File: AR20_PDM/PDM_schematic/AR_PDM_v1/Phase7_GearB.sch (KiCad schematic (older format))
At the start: 12 parts, among them Q7 BTS50025-1TAD, U11 INA233

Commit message: Alpha version DONE! - Gerber files generated
- Tweeked
- checked and re cheked
- added all missing components
- Created a really nice silkscreen
- Ready To Test
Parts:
- renumbered C12 to C37, C_out6 to C38, C13 to C39, C14 to C40, C15 to C41, Q7 to Q8, R12 to R35, R_in6 to R36, R_sense6 to R37, R13 to R38, R_Shunt10 to R39, U11 to U8

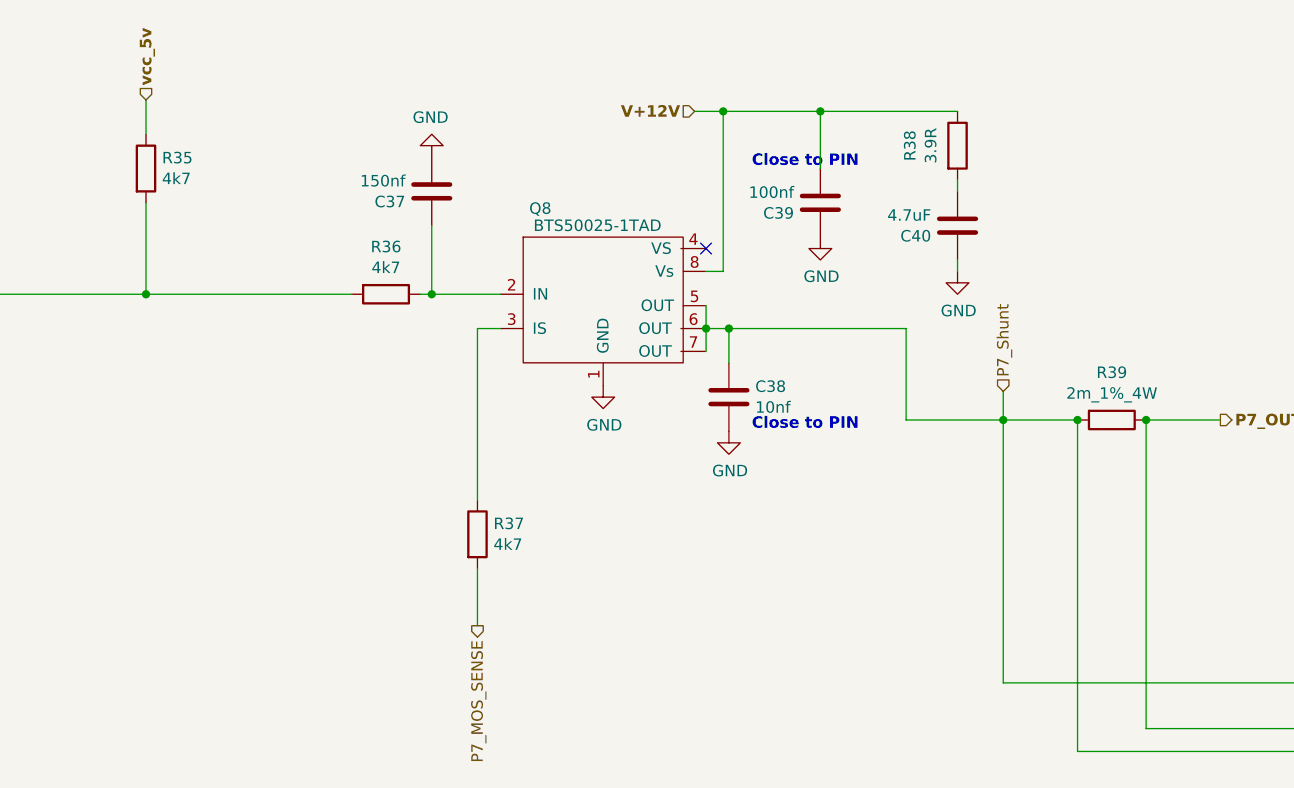
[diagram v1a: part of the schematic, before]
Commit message: Fixed wrong resistors, mos sense. Gerber files updated
- removed all R_is_protection resistors on each mosfet line
- added one R_is_protection resistors to mos_sense_all
ps, mux N-fets, does not need overvoltage protection. 60 volt tolerant.
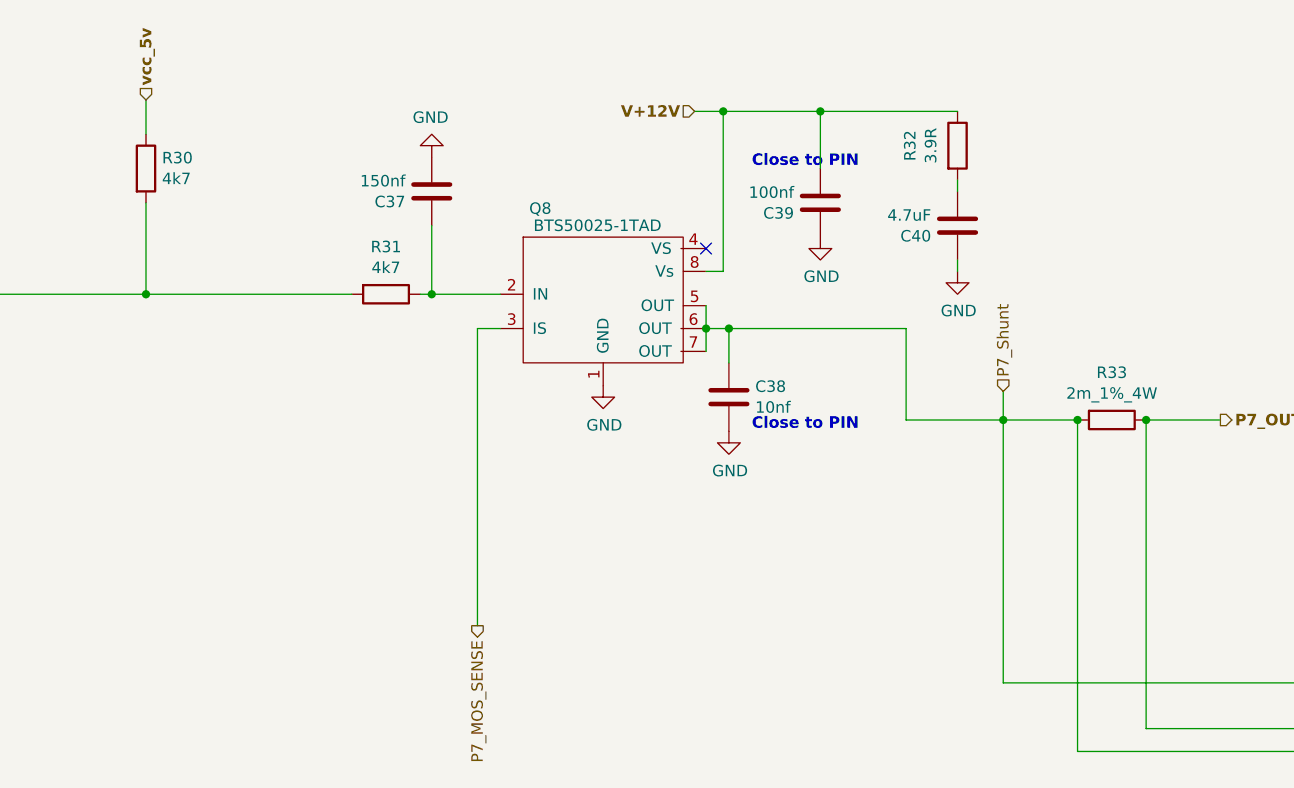
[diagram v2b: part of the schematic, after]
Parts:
- removed R37: 4k7, Resistor_SMD:R_0603_1608Metric, symbol AR20_PDM_v1-rescue:R-Device
- renumbered R35 to R30, R36 to R31, R38 to R32, R39 to R33
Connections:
- net P7_MOS_SENSE: now also Q8.3 (IS)
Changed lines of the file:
@@
 AR Path="/5E0FCFDC/5DAAC1B1" Ref="R?"  Part="1"
 AR Path="/5E0FDCCC/5DAAC1B1" Ref="R?"  Part="1"
-AR Path="/5E10174B/5DAAC1B1" Ref="R36"  Part="1"
-F 0 "R36" V 3093 2400 50  0000 C CNN
+AR Path="/5E10174B/5DAAC1B1" Ref="R31"  Part="1"
+F 0 "R31" V 3093 2400 50  0000 C CNN
 F 1 "4k7" V 3184 2400 50  0000 C CNN
 F 2 "Resistor_SMD:R_0603_1608Metric" V 3230 2400 50  0001 C CNN
@@
 AR Path="/5E0FCFDC/5E21B81A" Ref="R?"  Part="1"
 AR Path="/5E0FDCCC/5E21B81A" Ref="R?"  Part="1"
-AR Path="/5E10174B/5E21B81A" Ref="R35"  Part="1"
-F 0 "R35" H 2320 1896 50  0000 L CNN
+AR Path="/5E10174B/5E21B81A" Ref="R30"  Part="1"
+F 0 "R30" H 2320 1896 50  0000 L CNN
 F 1 "4k7" H 2320 1805 50  0000 L CNN
 F 2 "Resistor_SMD:R_0603_1608Metric" V 2180 1850 50  0001 C CNN
@@
 	3700 2550 3800 2550
 Wire Wire Line
-	3700 3850 3700 3600
-Wire Wire Line
 	8750 2850 8750 3350
 Wire Wire Line
@@
 AR Path="/5E0FCFDC/5DB84D30" Ref="R?"  Part="1"
 AR Path="/5E0FDCCC/5DB84D30" Ref="R?"  Part="1"
-AR Path="/5E10174B/5DB84D30" Ref="R38"  Part="1"
-F 0 "R38" V 5593 1750 50  0000 C CNN
+AR Path="/5E10174B/5DB84D30" Ref="R32"  Part="1"
+F 0 "R32" V 5593 1750 50  0000 C CNN
 F 1 "3.9R" V 5684 1750 50  0000 C CNN
 F 2 "Resistor_SMD:R_0603_1608Metric" V 5730 1750 50  0001 C CNN
@@
 AR Path="/5E0FCFDC/5E1DEBF3" Ref="R?"  Part="1"
 AR Path="/5E0FDCCC/5E1DEBF3" Ref="R?"  Part="1"
-AR Path="/5E10174B/5E1DEBF3" Ref="R39"  Part="1"
-F 0 "R39" V 6268 2950 50  0000 C CNN
+AR Path="/5E10174B/5E1DEBF3" Ref="R33"  Part="1"
+F 0 "R33" V 6268 2950 50  0000 C CNN
 F 1 "2m_1%_4W" V 6359 2950 50  0000 C CNN
 F 2 "Resistor_SMD:R_2512_6332Metric" V 6405 2950 50  0001 C CNN
@@
 P7_Shunt
 Connection ~ 6000 2950
-Wire Wire Line
-	3700 2550 3700 3300
-$Comp
-L AR20_PDM_v1-rescue:R-Device R?
-U 1 1 5E0E437E
-P 3700 3450
-AR Path="/5DA89415/5E0E437E" Ref="R?"  Part="1"
-AR Path="/5DEB10A1/5E0E437E" Ref="R?"  Part="1"
-AR Path="/5DEB20EA/5E0E437E" Ref="R?"  Part="1"
-AR Path="/5E0E4725/5E0E437E" Ref="R?"  Part="1"
-AR Path="/5E0E4A93/5E0E437E" Ref="R?"  Part="1"
-AR Path="/5E0E4EB5/5E0E437E" Ref="R?"  Part="1"
-AR Path="/5E0E5304/5E0E437E" Ref="R?"  Part="1"
-AR Path="/5E0E594B/5E0E437E" Ref="R?"  Part="1"
-AR Path="/5E0E607C/5E0E437E" Ref="R?"  Part="1"
-AR Path="/5E0FB5C8/5E0E437E" Ref="R?"  Part="1"
-AR Path="/5E0FBBBD/5E0E437E" Ref="R?"  Part="1"
-AR Path="/5E0FC3A2/5E0E437E" Ref="R?"  Part="1"
-AR Path="/5E0FCFDC/5E0E437E" Ref="R?"  Part="1"
-AR Path="/5E0FDCCC/5E0E437E" Ref="R?"  Part="1"
-AR Path="/5E10174B/5E0E437E" Ref="R37"  Part="1"
-F 0 "R37" H 3770 3496 50  0000 L CNN
-F 1 "4k7" H 3770 3405 50  0000 L CNN
-F 2 "Resistor_SMD:R_0603_1608Metric" V 3630 3450 50  0001 C CNN
-F 3 "~" H 3700 3450 50  0001 C CNN
-	1    3700 3450
-	1    0    0    -1
-$EndComp
 Text HLabel 3700 3850 3    50   Output ~ 0
 P7_MOS_SENSE
@@
 Wire Wire Line
 	4775 1600 5200 1600
+Wire Wire Line
+	3700 2550 3700 3850
 $EndSCHEMATC

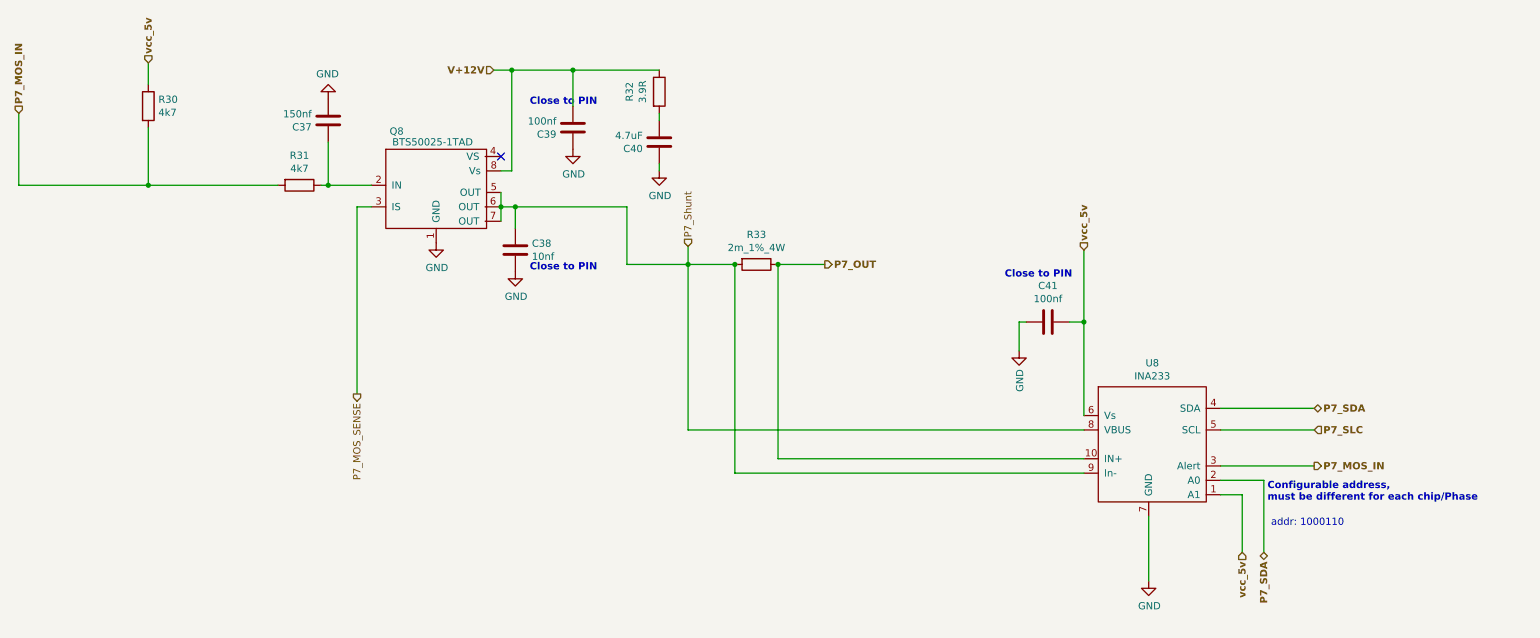
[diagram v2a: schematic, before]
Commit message: Major redesign. schematics completed, PCB work in progress
-TODO : A proper changelog file. Where all changes will apear 
- Redesigned schematics to accommodate errors in the improvement list
- More detail in ALPHA improvement list
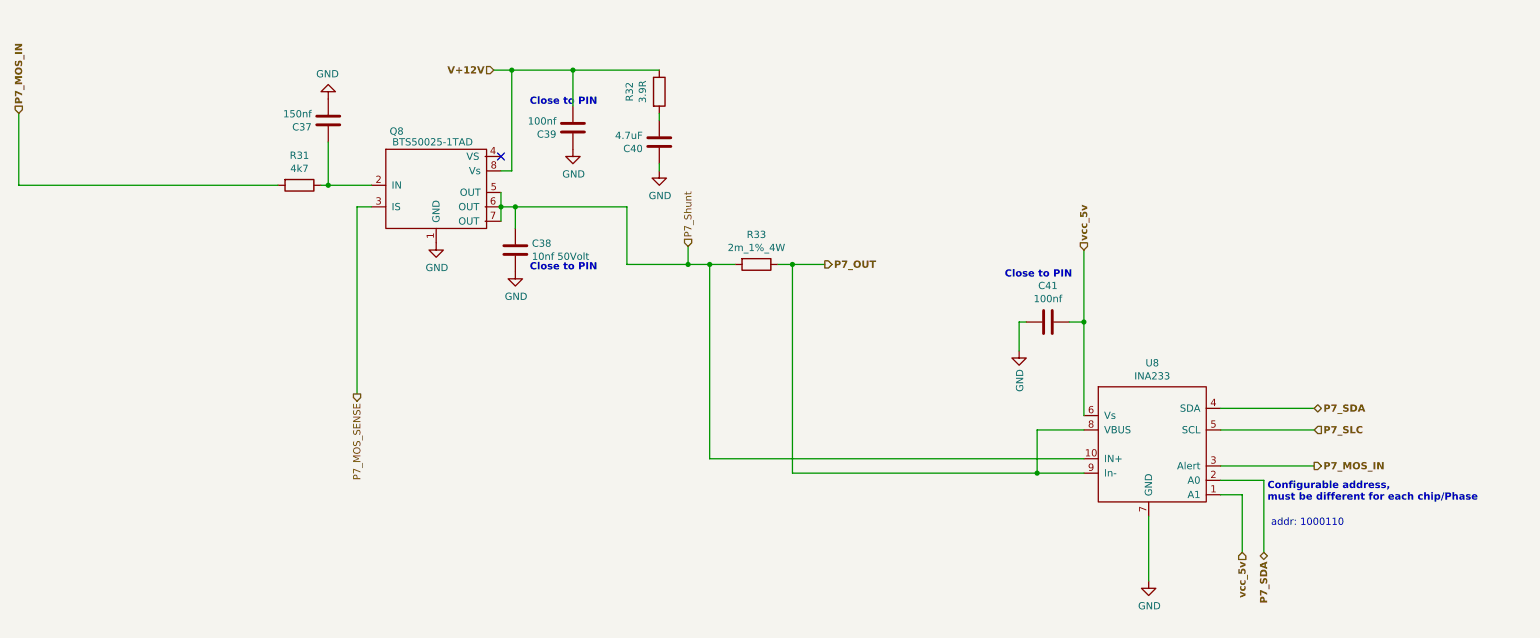
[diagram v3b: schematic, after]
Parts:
- removed R30: 4k7, Resistor_SMD:R_0603_1608Metric, symbol AR20_PDM_v1-rescue:R-Device
- C38: value 10nf -> 10nf 50Volt
- R32: footprint Resistor_SMD:R_0603_1608Metric -> Resistor_SMD:R_2512_6332Metric
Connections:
- net P7_OUT: now also U8.8 (VBUS), U8.9 (In-); no longer U8.10 (IN+)
- net P7_Shunt: now also U8.10 (IN+); no longer U8.8 (VBUS), U8.9 (In-)
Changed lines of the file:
@@
 $Descr A4 11693 8268
 encoding utf-8
-Sheet 8 13
+Sheet 8 14
 Title ""
 Date ""
@@
 AR Path="/5E10174B/5E21B80D" Ref="C38"  Part="1"
 F 0 "C38" H 4915 2896 50  0000 L CNN
-F 1 "10nf" H 4915 2805 50  0000 L CNN
+F 1 "10nf 50Volt" H 4915 2805 50  0000 L CNN
 F 2 "Capacitor_SMD:C_0603_1608Metric" H 4838 2700 50  0001 C CNN
 F 3 "~" H 4800 2850 50  0001 C CNN
@@
 $EndComp
 $Comp
-L AR20_PDM_v1-rescue:R-Device R?
-U 1 1 5E21B81A
-P 2250 1850
-AR Path="/5DA89415/5E21B81A" Ref="R?"  Part="1"
-AR Path="/5DEB10A1/5E21B81A" Ref="R?"  Part="1"
-AR Path="/5DEB20EA/5E21B81A" Ref="R?"  Part="1"
-AR Path="/5E0E4725/5E21B81A" Ref="R?"  Part="1"
-AR Path="/5E0E4A93/5E21B81A" Ref="R?"  Part="1"
-AR Path="/5E0E4EB5/5E21B81A" Ref="R?"  Part="1"
-AR Path="/5E0E5304/5E21B81A" Ref="R?"  Part="1"
-AR Path="/5E0E594B/5E21B81A" Ref="R?"  Part="1"
-AR Path="/5E0E607C/5E21B81A" Ref="R?"  Part="1"
-AR Path="/5E0FB5C8/5E21B81A" Ref="R?"  Part="1"
-AR Path="/5E0FBBBD/5E21B81A" Ref="R?"  Part="1"
-AR Path="/5E0FC3A2/5E21B81A" Ref="R?"  Part="1"
-AR Path="/5E0FCFDC/5E21B81A" Ref="R?"  Part="1"
-AR Path="/5E0FDCCC/5E21B81A" Ref="R?"  Part="1"
-AR Path="/5E10174B/5E21B81A" Ref="R30"  Part="1"
-F 0 "R30" H 2320 1896 50  0000 L CNN
-F 1 "4k7" H 2320 1805 50  0000 L CNN
-F 2 "Resistor_SMD:R_0603_1608Metric" V 2180 1850 50  0001 C CNN
-F 3 "~" H 2250 1850 50  0001 C CNN
-	1    2250 1850
-	1    0    0    -1
-$EndComp
-$Comp
 L AR20_PDM_v1-rescue:C-Device C?
 U 1 1 5E21B826
@@
 Text Notes 8200 3050 0    50   ~ 10
 Close to PIN
-Text HLabel 2250 1550 1    50   Input ~ 10
-vcc_5v
 Wire Wire Line
 	9700 4100 10350 4100
-Wire Wire Line
-	2250 1550 2250 1700
 $Comp
 L AR20_PDM_v1-rescue:C-Device C?
@@
 F 0 "R32" V 5593 1750 50  0000 C CNN
 F 1 "3.9R" V 5684 1750 50  0000 C CNN
-F 2 "Resistor_SMD:R_0603_1608Metric" V 5730 1750 50  0001 C CNN
+F 2 "Resistor_SMD:R_2512_6332Metric" V 5730 1750 50  0001 C CNN
 F 3 "~" H 5800 1750 50  0001 C CNN
 	1    5800 1750
@@
 Wire Wire Line
 	9700 4350 10350 4350
-Connection ~ 2250 2400
-Wire Wire Line
-	2250 2000 2250 2400
 Wire Wire Line
 	1350 1900 1350 2400
-Wire Wire Line
-	1350 2400 2250 2400
 Wire Wire Line
 	10000 4450 10000 4950
@@
 	5575 2550 5575 2950
 Connection ~ 4800 2550
-Wire Wire Line
-	6000 4100 8750 4100
-Wire Wire Line
-	6625 4300 8750 4300
-Wire Wire Line
-	6000 4100 6000 2950
 Wire Wire Line
 	5575 2950 6000 2950
@@
 V+12V
 Wire Wire Line
-	2250 2400 3150 2400
-Wire Wire Line
-	6625 2950 6625 4300
-Wire Wire Line
-	6325 2950 6325 4400
-Wire Wire Line
-	6000 2950 6325 2950
+	6000 2950 6150 2950
 $Comp
 L AR20_PDM_v1-rescue:R-Device R?
@@
 $EndComp
 Wire Wire Line
-	6625 2950 6950 2950
-Connection ~ 6325 2950
-Connection ~ 6625 2950
+	6625 2950 6725 2950
 Text Notes 10050 4775 0    50   ~ 0
 addr: 1000110
@@
 Text HLabel 9850 4950 3    50   Input ~ 10
 vcc_5v
-Wire Wire Line
-	6325 4400 8750 4400
 Text HLabel 10000 4950 3    50   BiDi ~ 10
 P7_SDA
@@
 Wire Wire Line
 	3700 2550 3700 3850
+Wire Wire Line
+	1350 2400 3150 2400
+Wire Wire Line
+	8750 4300 6150 4300
+Wire Wire Line
+	6150 4300 6150 2950
+Wire Wire Line
+	8750 4400 8425 4400
+Wire Wire Line
+	6725 4400 6725 2950
+Wire Wire Line
+	8750 4100 8425 4100
+Wire Wire Line
+	8425 4100 8425 4400
+Connection ~ 8425 4400
+Wire Wire Line
+	8425 4400 6725 4400
+Connection ~ 6150 2950
+Wire Wire Line
+	6150 2950 6325 2950
+Connection ~ 6725 2950
+Wire Wire Line
+	6725 2950 6950 2950
 $EndSCHEMATC

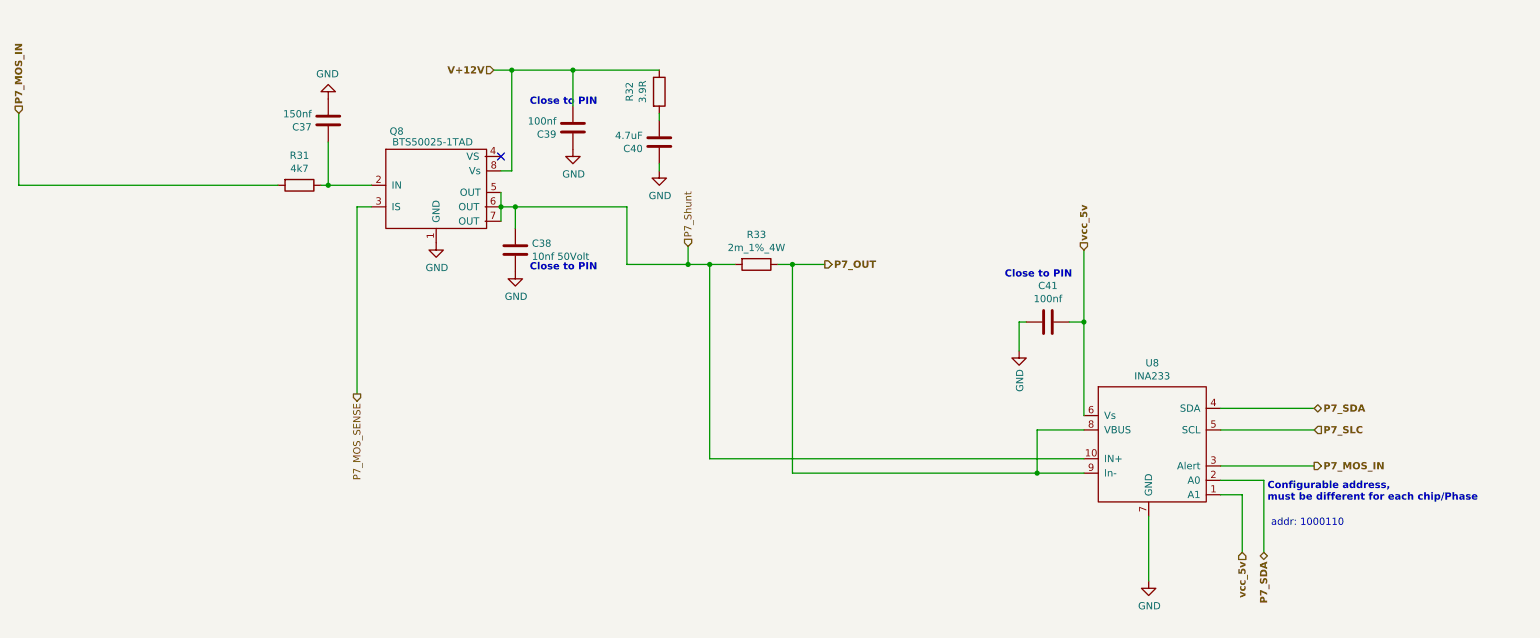
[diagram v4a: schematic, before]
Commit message: schematics rework
Fixed INA233 frying due to inductive flyback:
- Paced ina233 high side of the mosftets
- New input protection reseistors, and zener diodes, on each ina233.
Simplified:
- Removed the MUX and mos sense lines, as i realize that most of this functionality can be obtained trough INA233.
- Removed some of the cappacitors , besides the most needed ones.
- removed  back to back zener diode configuration, now a single diode insted.
 to reduce negative voltage in case of loss of VS, to be easy on the INA233 filters.
new stuff:
- Another temp sensor.
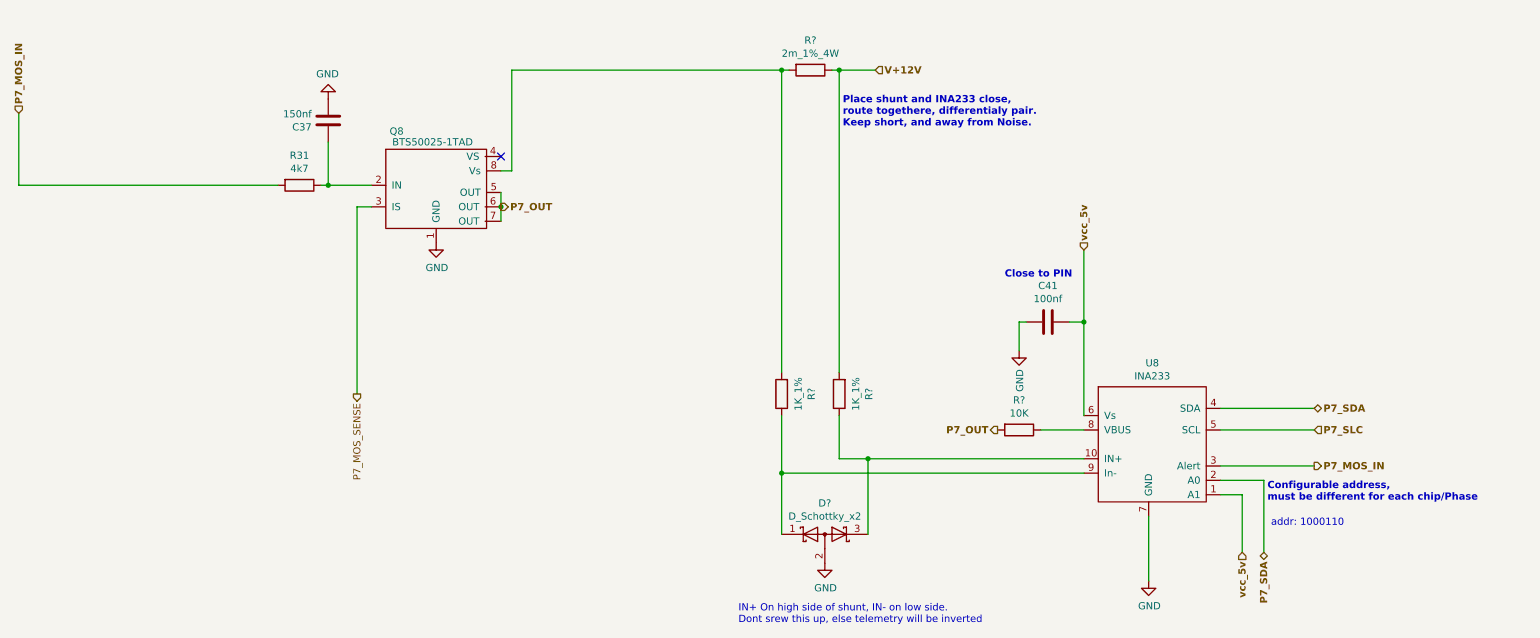
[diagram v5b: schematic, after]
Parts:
- removed C38: 10nf 50Volt, Capacitor_SMD:C_0603_1608Metric, symbol AR20_PDM_v1-rescue:C-Device
- removed C39: 100nf, Capacitor_SMD:C_0603_1608Metric, symbol AR20_PDM_v1-rescue:C-Device
- removed C40: 4.7uF, Capacitor_SMD:C_1206_3216Metric, symbol AR20_PDM_v1-rescue:C-Device
- removed R32: 3.9R, Resistor_SMD:R_2512_6332Metric, symbol AR20_PDM_v1-rescue:R-Device
- removed R33: 2m_1%_4W, Resistor_SMD:R_2512_6332Metric, symbol AR20_PDM_v1-rescue:R-Device
- added D?: D_Schottky_x2, symbol AR20_PDM_v1-rescue:D_Schottky_x2
- added R?: 2m_1%_4W, Resistor_SMD:R_2512_6332Metric, symbol AR20_PDM_v1-rescue:R-Device
- added R? (x2): 1K_1%, Resistor_SMD:R_0603_1608Metric, symbol AR20_PDM_v1-rescue:R-Device
- added R?: 10K, Resistor_SMD:R_0603_1608Metric, symbol AR20_PDM_v1-rescue:R-Device
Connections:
- net GND: now also D?.2 (A)
- net P7_OUT: now also Q8.5 (OUT), Q8.6 (OUT), Q8.7 (OUT), R?.2; no longer U8.8 (VBUS), U8.9 (In-)
- net V+12V: now also R?.1, R?.2; no longer Q8.8 (Vs)
- removed net P7_Shunt: Q8.5 (OUT), Q8.6 (OUT), Q8.7 (OUT), U8.10 (IN+)
- new net: Q8.8 (Vs), R?.2, R?.2
- new net: D?.3 (K), R?.1, U8.10 (IN+)
- new net: R?.1, U8.8 (VBUS)
- new net: D?.1 (K), R?.1, U8.9 (In-)
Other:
- note added: "IN+ On high side of shunt, IN- on low side.\nDont srew this up, else telemetry will be inverted"
- note added: "Place shunt and INA233 close, \nroute togethere, differentialy pair. \nKeep short, and away from Noise."
